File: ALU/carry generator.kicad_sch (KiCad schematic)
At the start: 26 parts, among them U10 74HCT21, U11 74AHCT1G02, U12 74AHCT1G02, U13 74AHC1G08, U14 74AHC1G08, U15 74AHCT1G02, U16 74AHCT1G02, U19 74AHC1G08, U20 74AHCT1G02, U21 74AHCT1G02, U3 74AHC1G04, U6 74AHC1G08, U7 74HCT11

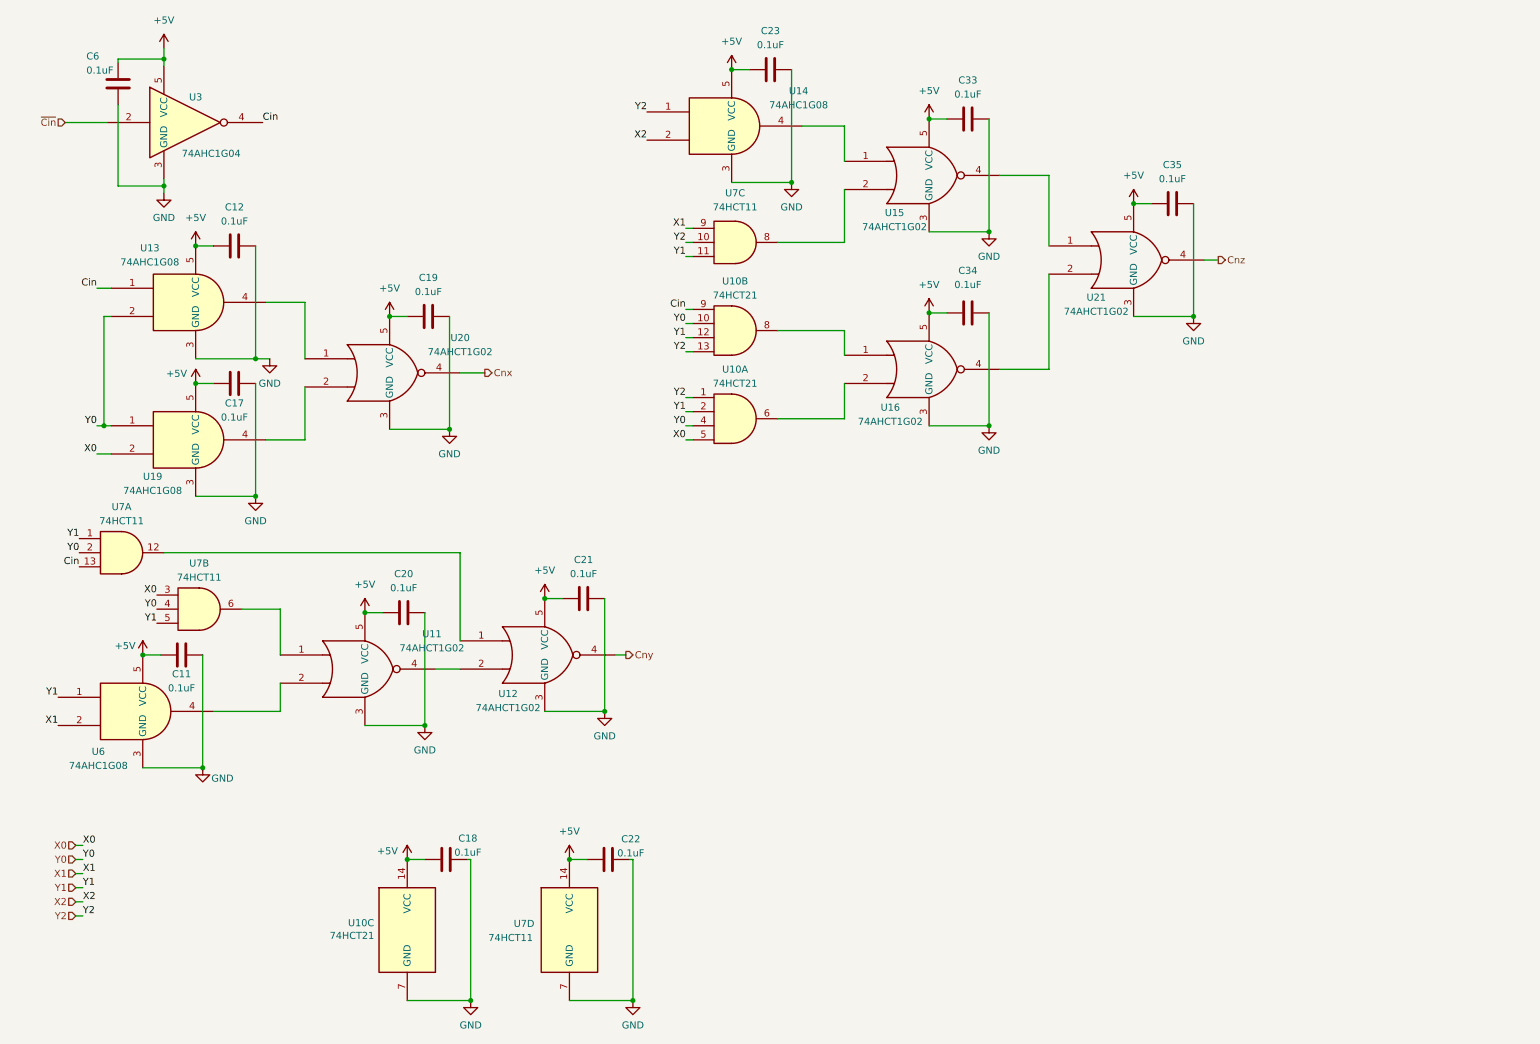
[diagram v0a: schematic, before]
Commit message: Updated ALU and moved common schematics to common/ for enhanced reusability
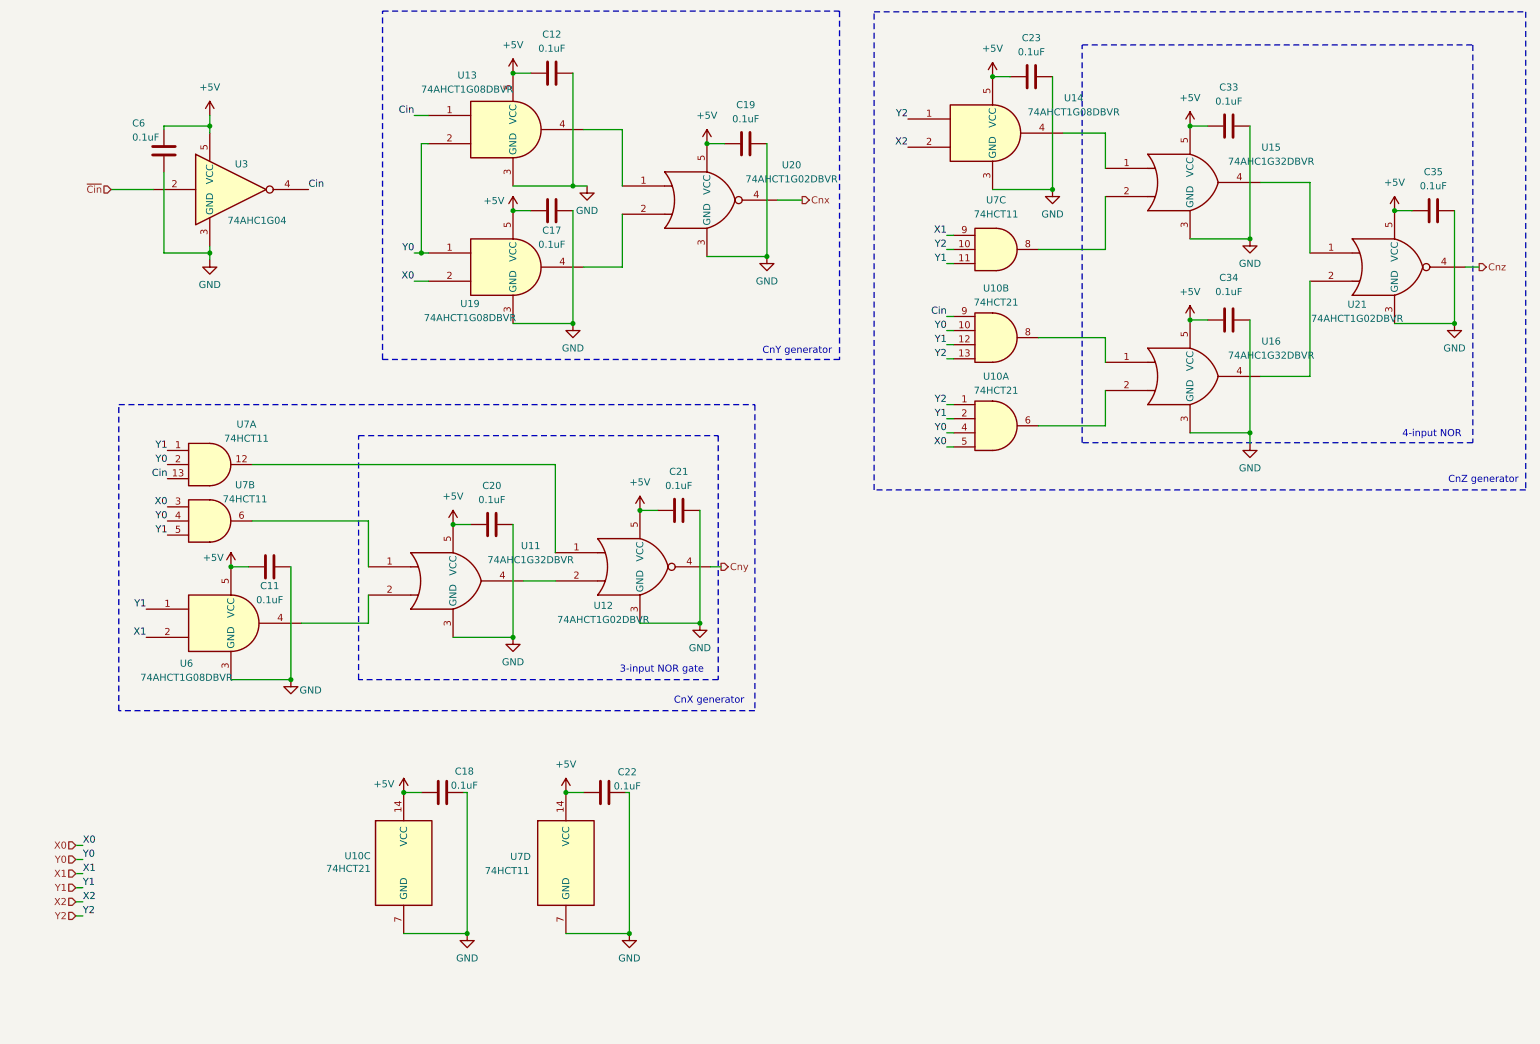
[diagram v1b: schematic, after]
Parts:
- removed U11, U15, U16: 74AHCT1G02, Package_TO_SOT_SMD:SOT-353_SC-70-5, symbol 74xGxx:74AHCT1G02
- added U11, U15, U16: 74AHC1G32DBVR, Package_TO_SOT_SMD:SOT-23-5, symbol 74xGxx:74AHC1G32
- U12, U20, U21: value 74AHCT1G02 -> 74AHCT1G02DBVR; footprint Package_TO_SOT_SMD:SOT-353_SC-70-5 -> Package_TO_SOT_SMD:SOT-23-5
- U13, U14, U19, U6: value 74AHC1G08 -> 74AHCT1G08DBVR; footprint Package_TO_SOT_SMD:SOT-353_SC-70-5 -> Package_TO_SOT_SMD:SOT-23-5
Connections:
- net +5V: now also U11.5 (VCC), U15.5 (VCC), U16.5 (VCC)
- net GND: now also U11.3 (GND), U15.3 (GND), U16.3 (GND)
- net at U10.8: now also U16.1
- net at U10.6: now also U16.2
- net at U21.2: now also U16.4
- net at U14.4: now also U15.1
- net at U7.8: now also U15.2
- net at U21.1: now also U15.4
- net at U6.4: now also U11.2
- net at U7.6: now also U11.1
- net at U12.2: now also U11.4
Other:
- note added: "3-input NOR gate"
- note added: "4-input NOR"
- note added: "CnX generator"
- note added: "CnY generator"
- note added: "CnZ generator"
- title: (none) -> Full Lookahead Carry Generator
- moved on the sheet: C11, C12, C17, C18, C19, C20, C21, C22, C23, C33, C34, C35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

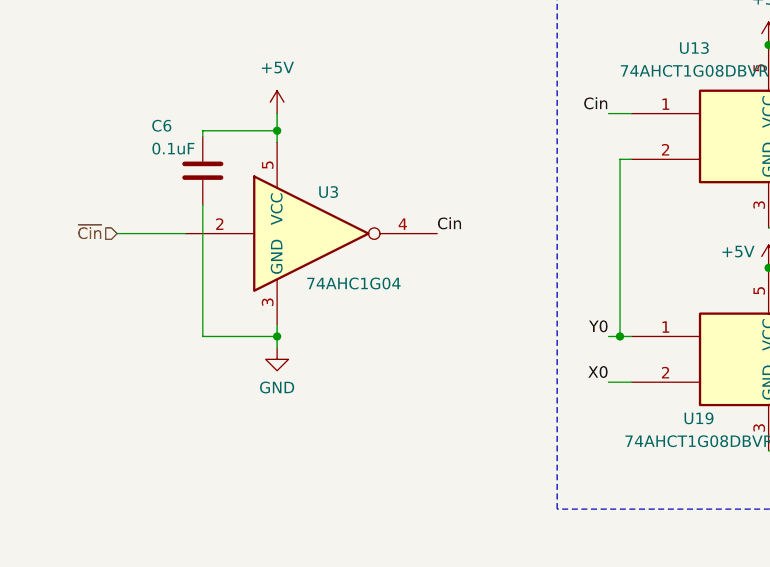
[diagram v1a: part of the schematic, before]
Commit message: Fixed ALU silkscreen for new fab
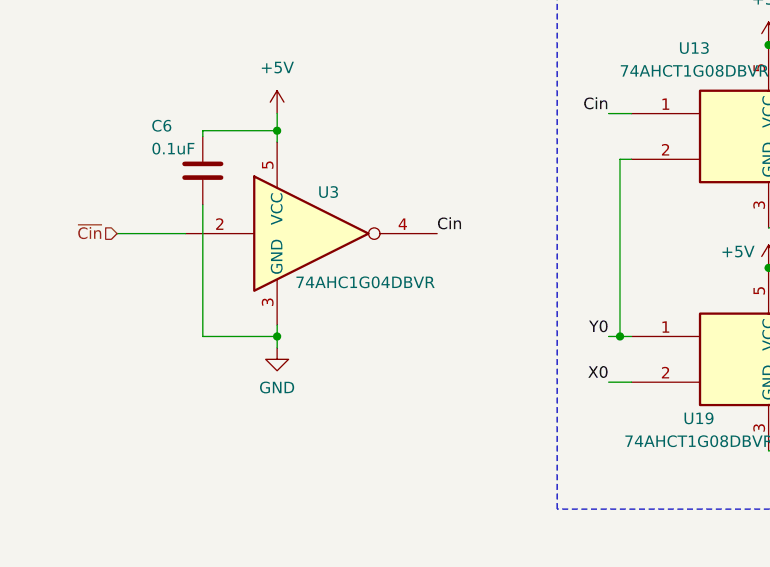
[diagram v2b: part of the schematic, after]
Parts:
- U3: value 74AHC1G04 -> 74AHC1G04DBVR
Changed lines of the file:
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@@
 			)
 		)
-		(property "Value" "74AHC1G04"
-			(at 52.324 51.943 0)
+		(property "Value" "74AHC1G04DBVR"
+			(at 53.594 51.816 0)
 			(effects
 				(font
